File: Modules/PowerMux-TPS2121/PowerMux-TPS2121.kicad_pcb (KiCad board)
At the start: 4 copper layers, 14 parts, among them U10 TPS2121RUXR

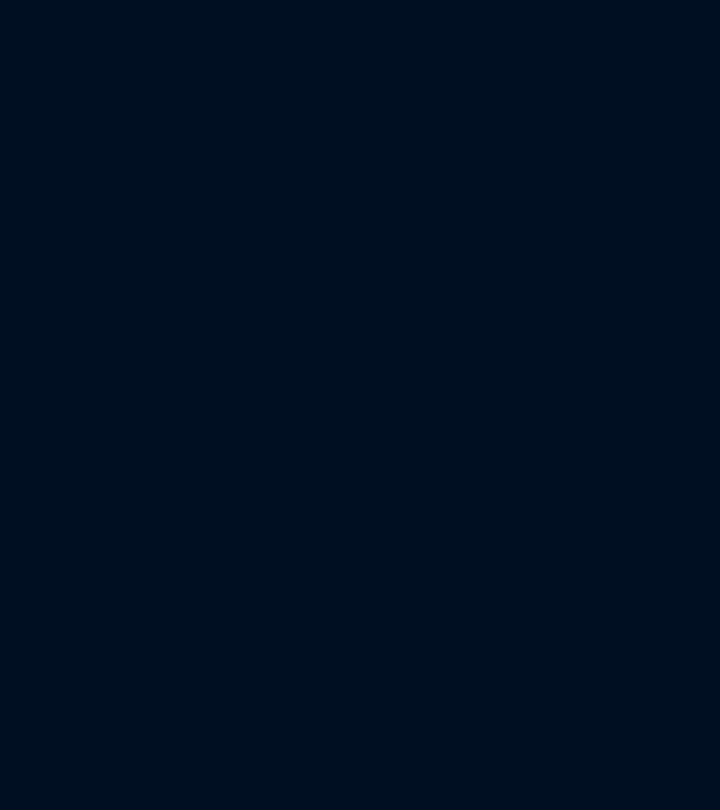
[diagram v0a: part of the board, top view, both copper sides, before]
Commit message: Add the base zones to five module boards
Whole-board zones for USBC, Buck, PowerMux, MCU and RF, written by file
before each board is opened. RF In1 carries a notch under J3 pad 1. Power
polygons become wide tracks during layout, because add_copper_pour cannot
set a zone priority.

Co-Authored-By: Claude Opus 5.5 (1M context) <noreply@anthropic.com>
Claude-Session: https://claude.ai/code/session_01ErAAfkmF4h3T5yfrw21utF
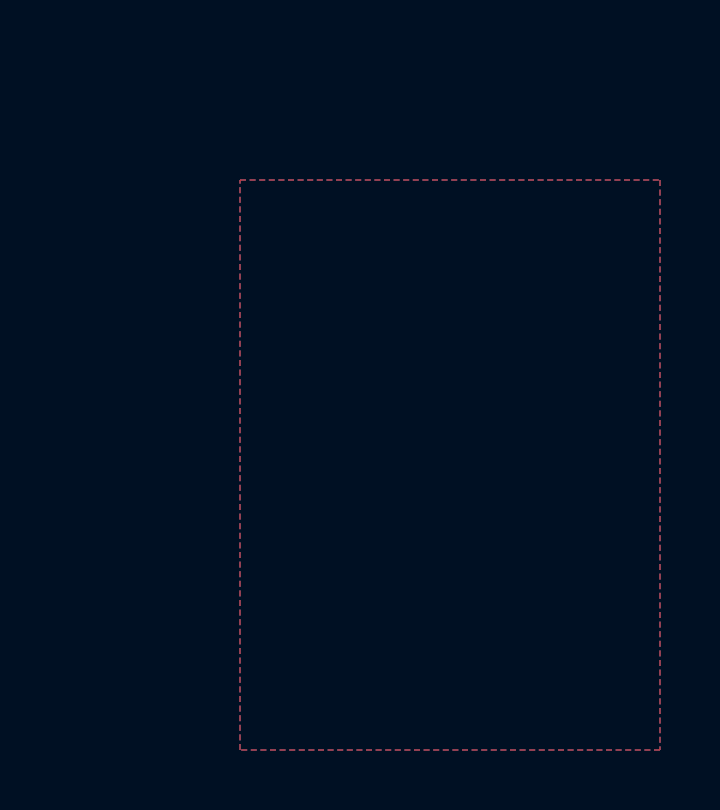
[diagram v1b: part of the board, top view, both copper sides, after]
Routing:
- added copper zone on In2.Cu, net /V5_SYS
- added copper zone on B.Cu, net GND
- added copper zone on F.Cu, net GND
- added copper zone on In1.Cu, net GND
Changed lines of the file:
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@@
 	)
 	(embedded_fonts no)
-)
+  (zone (net 0) (net_name "GND") (layer "F.Cu")
+    (hatch edge 0.508)
+    (connect_pads (clearance 0.2))
+    (min_thickness 0.25)
+    (fill yes)
+    (polygon (pts
+      (xy 100.5 100.5)
+      (xy 114.5 100.5)
+      (xy 114.5 119.5)
+      (xy 100.5 119.5)
+    ))
+  )
+  (zone (net 0) (net_name "GND") (layer "In1.Cu")
+    (hatch edge 0.508)
+    (connect_pads (clearance 0.2))
+    (min_thickness 0.25)
+    (fill yes)
+    (polygon (pts
+      (xy 100.5 100.5)
+      (xy 114.5 100.5)
+      (xy 114.5 119.5)
+      (xy 100.5 119.5)
+    ))
+  )
+  (zone (net 0) (net_name "/V5_SYS") (layer "In2.Cu")
+    (hatch edge 0.508)
+    (connect_pads (clearance 0.2))
+    (min_thickness 0.25)
+    (fill yes)
+    (polygon (pts
+      (xy 100.5 100.5)
+      (xy 114.5 100.5)
+      (xy 114.5 119.5)
+      (xy 100.5 119.5)
+    ))
+  )
+  (zone (net 0) (net_name "GND") (layer "B.Cu")
+    (hatch edge 0.508)
+    (connect_pads (clearance 0.2))
+    (min_thickness 0.25)
+    (fill yes)
+    (polygon (pts
+      (xy 100.5 100.5)
+      (xy 114.5 100.5)
+      (xy 114.5 119.5)
+      (xy 100.5 119.5)
+    ))
+  ))

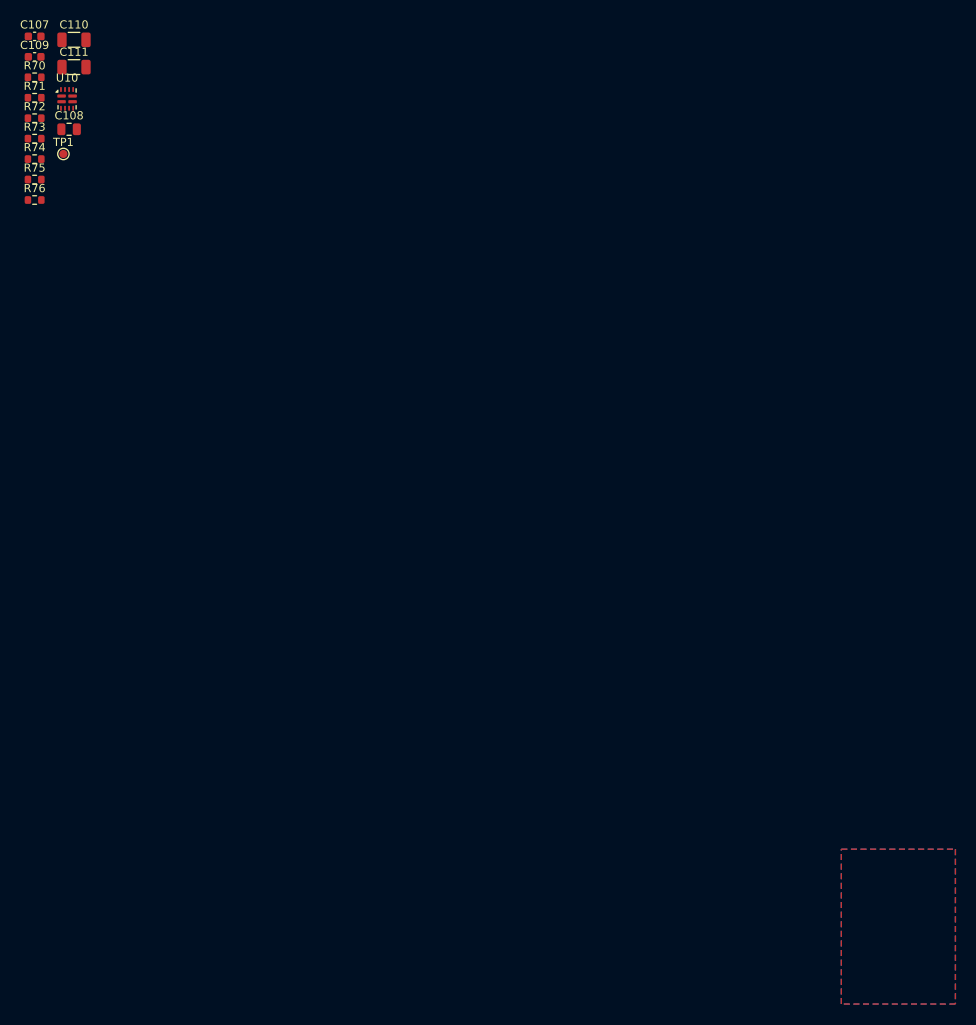
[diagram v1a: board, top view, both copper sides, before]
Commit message: Lay out the PowerMux-TPS2121 module
15 x 20 mm, 4 layers. The six divider resistors stand in one row above
U10, each node over its pin, so PR1, OV1 and OV2 route on F.Cu with no via
and no crossing. POE_5V and VBUS run F.Cu trunks at the board sides.
V5_SYS leaves each output cap through three vias to the In2 plane.
Breakout row: POE_5V, GND, V5_SYS, GND, VBUS, three vias per power net.

DRC: 0 errors, 0 unconnected, 0 parity. The 9 track_dangling warnings are
the 9 interface stubs. Canary 57 to 417.

One lib_footprint_mismatch on U10: Konnect rotate_component drops the
footprint's (units) block. Pads are unchanged. Update Footprint from
Library in GUI batch 2 restores it.

Co-Authored-By: Claude Opus 5.5 (1M context) <noreply@anthropic.com>
Claude-Session: https://claude.ai/code/session_01ErAAfkmF4h3T5yfrw21utF
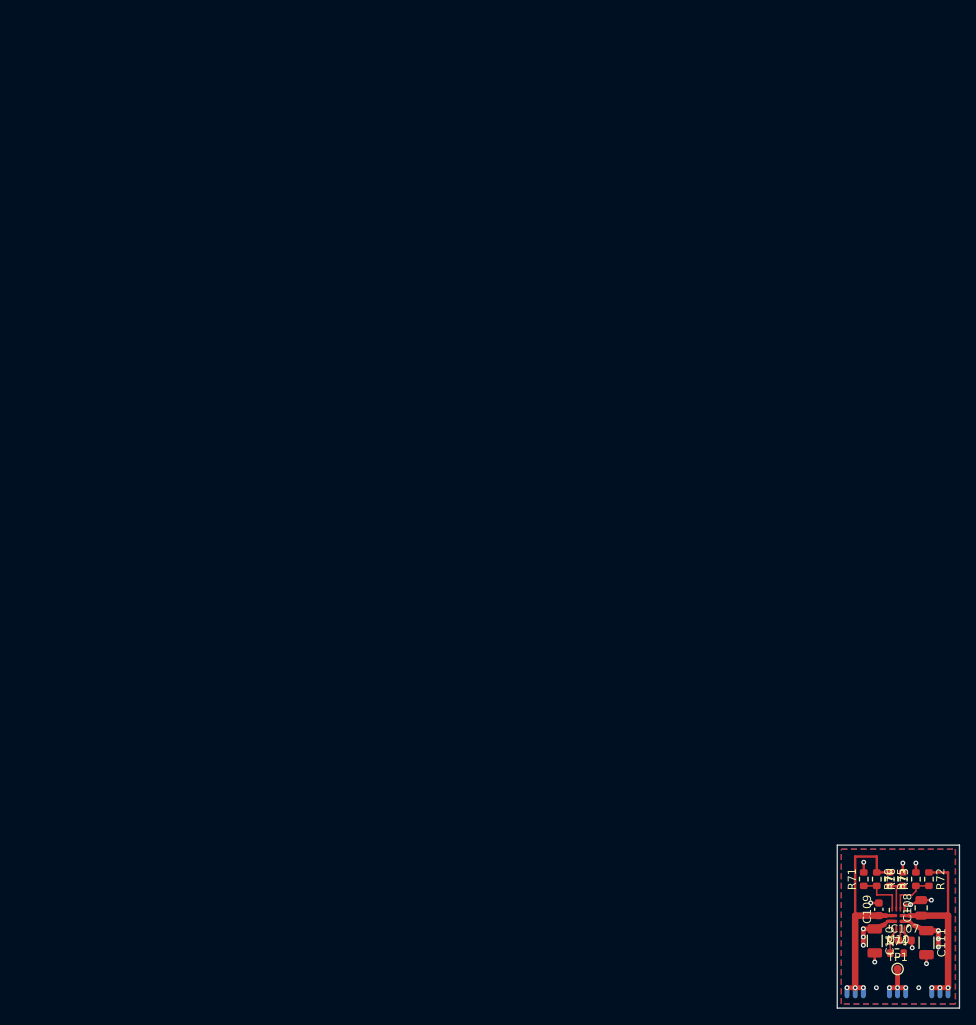
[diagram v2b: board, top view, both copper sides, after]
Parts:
- moved C107 154.0 mm to (108.3, 111.7)
- moved C111 150.0 mm to (111.0, 112.0), turned to -90 degrees
- moved C110 147.9 mm to (104.6, 111.8), turned to -90 degrees
- moved C109 147.2 mm to (105.1, 107.9), turned to 90 degrees
- moved R72 144.1 mm to (111.2, 104.2), turned to -90 degrees
- moved R74 143.8 mm to (107.3, 113.2)
- moved U10 143.3 mm to (107.5, 109.0), turned to 180 degrees
- moved TP1 143.1 mm to (107.4, 115.2)
- moved R70 142.7 mm to (104.8, 104.2), turned to -90 degrees
- moved C108 141.6 mm to (110.3, 107.7), turned to 90 degrees
- moved R73 141.3 mm to (109.7, 104.2), turned to 90 degrees
- moved R71 139.8 mm to (103.2, 104.2), turned to 90 degrees
- moved R75 135.6 mm to (106.5, 104.2), turned to -90 degrees
- moved R76 135.3 mm to (108.0, 104.2), turned to 90 degrees
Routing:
- net /POE_5V: track 0.00 -> 31.9 mm, vias 0 -> 3
- net /VBUS: track 0.00 -> 26.9 mm, vias 0 -> 3
- net /V5_SYS: track 0.00 -> 19.8 mm, vias 0 -> 9
- net GND: track 0.00 -> 13.5 mm, vias 0 -> 11
- net /MUX_PR1: track 0.00 -> 6.35 mm
- net /MUX_OV2: track 0.00 -> 6.09 mm
- net /MUX_OV1: track 0.00 -> 4.45 mm
- net /MUX_ILIM: track 0.00 -> 3.41 mm
- net /MUX_SS: track 0.00 -> 1.59 mm
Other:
- board outline added: 15 x 20 mm
- board text added: "GND"
- board text added: "POE_5V"
- board text added: "V5_SYS"
- board text added: "VBUS"

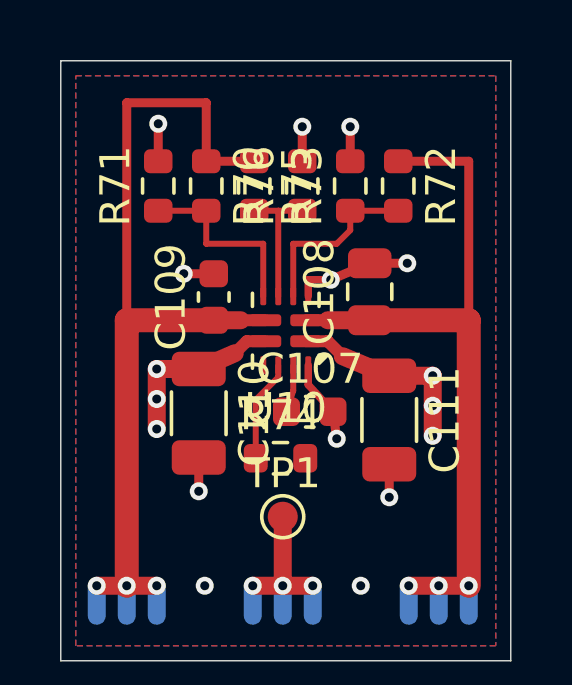
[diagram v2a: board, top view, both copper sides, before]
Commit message: Restore footprints and move passive references to F.Fab
GUI batch 2a on all eight module boards. Update Footprints from Library
restores the (units) blocks that Konnect IPC writes dropped: U10, U1, SW1,
SW2 and U4 no longer report lib_footprint_mismatch. Reference designators of
C, R, L, FB, D, Y and TP parts move to F.Fab. U, J and SW stay on the silk.

Every board: DRC 0 errors, 0 unconnected, 0 parity, the canary fires, and
track_dangling equals the interface stub count.

Co-Authored-By: Claude Opus 5.5 (1M context) <noreply@anthropic.com>
Claude-Session: https://claude.ai/code/session_01ErAAfkmF4h3T5yfrw21utF
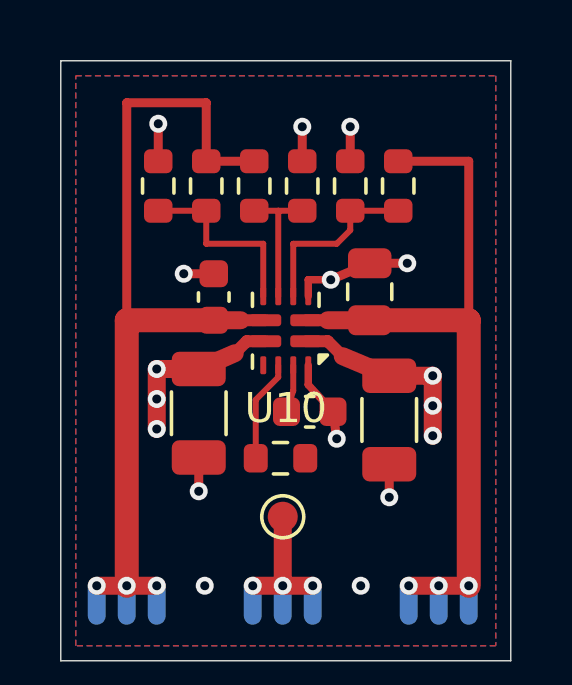
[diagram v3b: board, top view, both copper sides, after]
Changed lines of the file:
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@@
 		(tags "capacitor")
 		(property "Reference" "C111"
-			(at 0 -1.85 -90)
-			(layer "F.SilkS")
+			(at 0 -1.85 270)
+			(layer "F.Fab")
 			(effects
 				(font
@@
 		)
 		(property "Value" "47uF X5R"
-			(at 0 1.85 -90)
+			(at 0 1.85 270)
 			(layer "F.Fab")
 			(effects
@@
 		)
 		(property "Datasheet" ""
-			(at 0 0 -90)
+			(at 0 0 270)
 			(layer "F.Fab")
 			(hide yes)
@@
 		)
 		(property "Description" ""
-			(at 0 0 -90)
+			(at 0 0 270)
 			(layer "F.Fab")
 			(hide yes)
@@
 		)
 		(property "KiLib_Generator" "SMD_2terminal_chip_molded"
-			(at 0 0 -90)
+			(at 0 0 270)
 			(layer "F.SilkS")
 			(hide yes)
@@
 		)
 		(property "MPN" "CGA1206X5R476M160NT"
-			(at 0 0 -90)
+			(at 0 0 270)
 			(unlocked yes)
 			(layer "F.Fab")
@@
 		)
 		(property "Manufacturer" "TDK"
-			(at 0 0 -90)
+			(at 0 0 270)
 			(unlocked yes)
 			(layer "F.Fab")
@@
 		)
 		(fp_text user "${REFERENCE}"
-			(at 0 0 -90)
+			(at 0 0 270)
 			(layer "F.Fab")
 			(effects
@@
 		(tags "resistor")
 		(property "Reference" "R70"
-			(at 0 -1.43 -90)
-			(layer "F.SilkS")
+			(at 0 -1.43 270)
+			(layer "F.Fab")
 			(effects
 				(font
@@
 		)
 		(property "Value" "169k 1%"
-			(at 0 1.43 -90)
+			(at 0 1.43 270)
 			(layer "F.Fab")
 			(effects
@@
 		)
 		(property "Datasheet" ""
-			(at 0 0 -90)
+			(at 0 0 270)
 			(layer "F.Fab")
 			(hide yes)
@@
 		)
 		(property "Description" ""
-			(at 0 0 -90)
+			(at 0 0 270)
 			(layer "F.Fab")
 			(hide yes)
@@
 		)
 		(property "KiLib_Generator" "SMD_2terminal_chip_molded"
-			(at 0 0 -90)
+			(at 0 0 270)
 			(layer "F.SilkS")
 			(hide yes)
@@
 		)
 		(property "MPN" "RC0603FR-07169KL"
-			(at 0 0 -90)
+			(at 0 0 270)
 			(unlocked yes)
 			(layer "F.Fab")
@@
 		)
 		(property "Manufacturer" "Yageo"
-			(at 0 0 -90)
+			(at 0 0 270)
 			(unlocked yes)
 			(layer "F.Fab")
@@
 		)
 		(fp_text user "${REFERENCE}"
-			(at 0 0 -90)
+			(at 0 0 270)
 			(layer "F.Fab")
 			(effects
@@
 		(tags "resistor")
 		(property "Reference" "R75"
-			(at 0 -1.43 -90)
-			(layer "F.SilkS")
+			(at 0 -1.43 270)
+			(layer "F.Fab")
 			(effects
 				(font
@@
 		)
 		(property "Value" "46.4k 1%"
-			(at 0 1.43 -90)
+			(at 0 1.43 270)
 			(layer "F.Fab")
 			(effects
@@
 		)
 		(property "Datasheet" ""
-			(at 0 0 -90)
+			(at 0 0 270)
 			(layer "F.Fab")
 			(hide yes)
@@
 		)
 		(property "Description" ""
-			(at 0 0 -90)
+			(at 0 0 270)
 			(layer "F.Fab")
 			(hide yes)
@@
 		)
 		(property "KiLib_Generator" "SMD_2terminal_chip_molded"
-			(at 0 0 -90)
+			(at 0 0 270)
 			(layer "F.SilkS")
 			(hide yes)
@@
 		)
 		(property "MPN" "RC0603FR-0746K4L"
-			(at 0 0 -90)
+			(at 0 0 270)
 			(unlocked yes)
 			(layer "F.Fab")
@@
 		)
 		(property "Manufacturer" "Yageo"
-			(at 0 0 -90)
+			(at 0 0 270)
 			(unlocked yes)
 			(layer "F.Fab")
@@
 		)
 		(fp_text user "${REFERENCE}"
-			(at 0 0 -90)
+			(at 0 0 270)
 			(layer "F.Fab")
 			(effects
@@
 		(property "Reference" "C107"
 			(at 0 -1.43 0)
-			(layer "F.SilkS")
+			(layer "F.Fab")
 			(effects
 				(font
@@
 		(property "Reference" "R76"
 			(at 0 -1.43 90)
-			(layer "F.SilkS")
+			(layer "F.Fab")
 			(effects
 				(font
@@
 		(property "Reference" "C109"
 			(at 0 -1.43 90)
-			(layer "F.SilkS")
+			(layer "F.Fab")
 			(effects
 				(font
@@
 		(tags "resistor")
 		(property "Reference" "R72"
-			(at 0 -1.43 -90)
-			(layer "F.SilkS")
+			(at 0 -1.43 270)
+			(layer "F.Fab")
 			(effects
 				(font
@@
 		)
 		(property "Value" "46.4k 1%"
-			(at 0 1.43 -90)
+			(at 0 1.43 270)
 			(layer "F.Fab")
 			(effects
@@
 		)
 		(property "Datasheet" ""
-			(at 0 0 -90)
+			(at 0 0 270)
 			(layer "F.Fab")
 			(hide yes)
@@
 		)
 		(property "Description" ""
-			(at 0 0 -90)
+			(at 0 0 270)
 			(layer "F.Fab")
 			(hide yes)
@@
 		)
 		(property "KiLib_Generator" "SMD_2terminal_chip_molded"
-			(at 0 0 -90)
+			(at 0 0 270)
 			(layer "F.SilkS")
 			(hide yes)
@@
 		)
 		(property "MPN" "RC0603FR-0746K4L"
-			(at 0 0 -90)
+			(at 0 0 270)
 			(unlocked yes)
 			(layer "F.Fab")
@@
 		)
 		(property "Manufacturer" "Yageo"
-			(at 0 0 -90)
+			(at 0 0 270)
 			(unlocked yes)
 			(layer "F.Fab")
@@
 		)
 		(fp_text user "${REFERENCE}"
-			(at 0 0 -90)
+			(at 0 0 270)
 			(layer "F.Fab")
 			(effects
@@
 		(property "Reference" "C108"
 			(at 0 -1.68 90)
-			(layer "F.SilkS")
+			(layer "F.Fab")
 			(effects
 				(font
@@
 		(tags "capacitor")
 		(property "Reference" "C110"
-			(at 0 -1.85 -90)
-			(layer "F.SilkS")
+			(at 0 -1.85 270)
+			(layer "F.Fab")
 			(effects
 				(font
@@
 		)
 		(property "Value" "47uF X5R"
-			(at 0 1.85 -90)
+			(at 0 1.85 270)
 			(layer "F.Fab")
 			(effects
@@
 		)
 		(property "Datasheet" ""
-			(at 0 0 -90)
+			(at 0 0 270)
 			(layer "F.Fab")
 			(hide yes)
@@
 		)
 		(property "Description" ""
-			(at 0 0 -90)
+			(at 0 0 270)
 			(layer "F.Fab")
 			(hide yes)
@@
 		)
 		(property "KiLib_Generator" "SMD_2terminal_chip_molded"
-			(at 0 0 -90)
+			(at 0 0 270)
 			(layer "F.SilkS")
 			(hide yes)
@@
 		)
 		(property "MPN" "CGA1206X5R476M160NT"
-			(at 0 0 -90)
+			(at 0 0 270)
 			(unlocked yes)
 			(layer "F.Fab")
@@
 		)
 		(property "Manufacturer" "TDK"
-			(at 0 0 -90)
+			(at 0 0 270)
 			(unlocked yes)
 			(layer "F.Fab")
@@
 		)
 		(fp_text user "${REFERENCE}"
-			(at 0 0 -90)
+			(at 0 0 270)
 			(layer "F.Fab")
 			(effects
@@
 		(fp_poly
 			(pts
-				(xy -1.11 -0.81) (xy -1.39 -0.81) (xy -1.11 -1.09)
+				(xy -1.11 -0.81) (xy -1.39 -0.81) (xy -1.11 -1.09) (xy -1.11 -0.81)
 			)
 			(stroke
@@
 		)
 		(fp_text user "${REFERENCE}"
-			(at 0 0 -90)
+			(at 0 0 270)
 			(layer "F.Fab")
 			(effects
@@
 		(property "Reference" "TP1"
 			(at 0 -1.448 0)
-			(layer "F.SilkS")
+			(layer "F.Fab")
 			(effects
 				(font
@@
 		(property "Reference" "R73"
 			(at 0 -1.43 90)
-			(layer "F.SilkS")
+			(layer "F.Fab")
 			(effects
 				(font
@@
 		(property "Reference" "R74"
 			(at 0 -1.43 0)
-			(layer "F.SilkS")
+			(layer "F.Fab")
 			(effects
 				(font
@@
 		(property "Reference" "R71"
 			(at 0 -1.43 90)
-			(layer "F.SilkS")
-			(effects
-				(font
+			(layer "F.Fab")
+			(effects
+				(font
